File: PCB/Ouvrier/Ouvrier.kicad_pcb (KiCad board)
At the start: 2 copper layers, 52 x 54.5 mm, 17 parts, among them J1 Batterie, J2 VBAT Xiao, J3 DC 5V input, Q1 2N2222B, U1 XIAO-ESP32-S3-Plus-DIP, U2 BMP581, U3 UWB

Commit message: Ouvrier_V8
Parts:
- R3: value 330R -> 1k
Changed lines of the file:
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@@
 			)
 		)
-		(property "Value" "330R"
+		(property "Value" "1k"
 			(at 5.08 2.37 0)
 			(layer "F.Fab")

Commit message: gbr
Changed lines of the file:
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@@
 		(filling no)
 		(pcbplotparams
-			(layerselection 0x00000000_00000000_55555555_5755f5ff)
-			(plot_on_all_layers_selection 0x00000000_00000000_00000000_00000000)
+			(layerselection 0x00000000_00000000_55555555_57555555)
+			(plot_on_all_layers_selection 0x00000000_00000000_00000000_02000000)
 			(disableapertmacros no)
 			(usegerberextensions no)
@@
 			(outputformat 1)
 			(mirror no)
-			(drillshape 1)
+			(drillshape 0)
 			(scaleselection 1)
 			(outputdirectory "")
@@
 	(via
 		(at 141.5 90.5)
-		(size 1)
+		(size 1.1)
 		(drill 0.8)
 		(layers "F.Cu" "B.Cu")
@@
 	(via
 		(at 120.25 66.25)
-		(size 1)
+		(size 1.1)
 		(drill 0.8)
 		(layers "F.Cu" "B.Cu")

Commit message: Ouvrier_v9_changement_bmp
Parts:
- moved R3 26.9 mm to (122.9, 100.0)
- moved R1 25.2 mm to (96.0, 96.5), turned to 0 degrees
- moved LS2 17.2 mm to (115.0, 101.2)
- moved D2 8.94 mm to (133.0, 103.2), turned to -90 degrees
- moved U2 7.99 mm to (131.0, 93.0), turned to 180 degrees
- moved Q1 7.15 mm to (107.0, 102.8)
- moved D1 4.61 mm to (119.8, 86.4)
- moved C1 4.29 mm to (140.5, 96.0), turned to 90 degrees
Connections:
- U2 pad 2: Net-(U1-P1.13_D8_SCK) -> GNDREF
- U2 pad 3: GNDREF -> Net-(U1-P1.13_D8_SCK)
- U2 pad 5: Net-(U1-P1.14_D9_MISO) -> unconnected-(U2-INT-Pad5)
- U2 pad 7: unconnected-(U2-INT-Pad7) -> Net-(U1-P1.14_D9_MISO)
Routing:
- net Net-(D2-K): track 44.3 -> 3.28 mm
- net GNDREF: track 71.5 -> 38.3 mm, vias 1 -> 0
- net Net-(U1-P0.28_A2_D2): track 23.1 -> 47.7 mm
- net Net-(U1-P1.14_D9_MISO): track 45.6 -> 28.0 mm
- net +3V3: track 92.9 -> 105.5 mm
- net Net-(D1-A): track 15.0 -> 22.2 mm
- net Net-(U1-P0.29_A3_D3): track 27.1 -> 20.9 mm
- net Net-(U1-P0.04_A4_D4_SDA): track 42.9 -> 38.3 mm
- net Net-(Q1-B): track 8.28 -> 5.17 mm
- net Net-(U1-P1.13_D8_SCK): track 18.2 -> 19.7 mm
- net Net-(U1-P1.15_D10_MOSI): track 20.1 -> 18.8 mm
- net Net-(U1-P1.12_D7_RX): vias 1 -> 0

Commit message: Ouvrier_v10_PCB
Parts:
- removed C1: 100nF, Capacitor_SMD:C_0402_1005Metric_Pad0.74x0.62mm_HandSolder
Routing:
- net GNDREF: track 38.3 -> 35.2 mm
- net +3V3: track 105.5 -> 104.7 mm

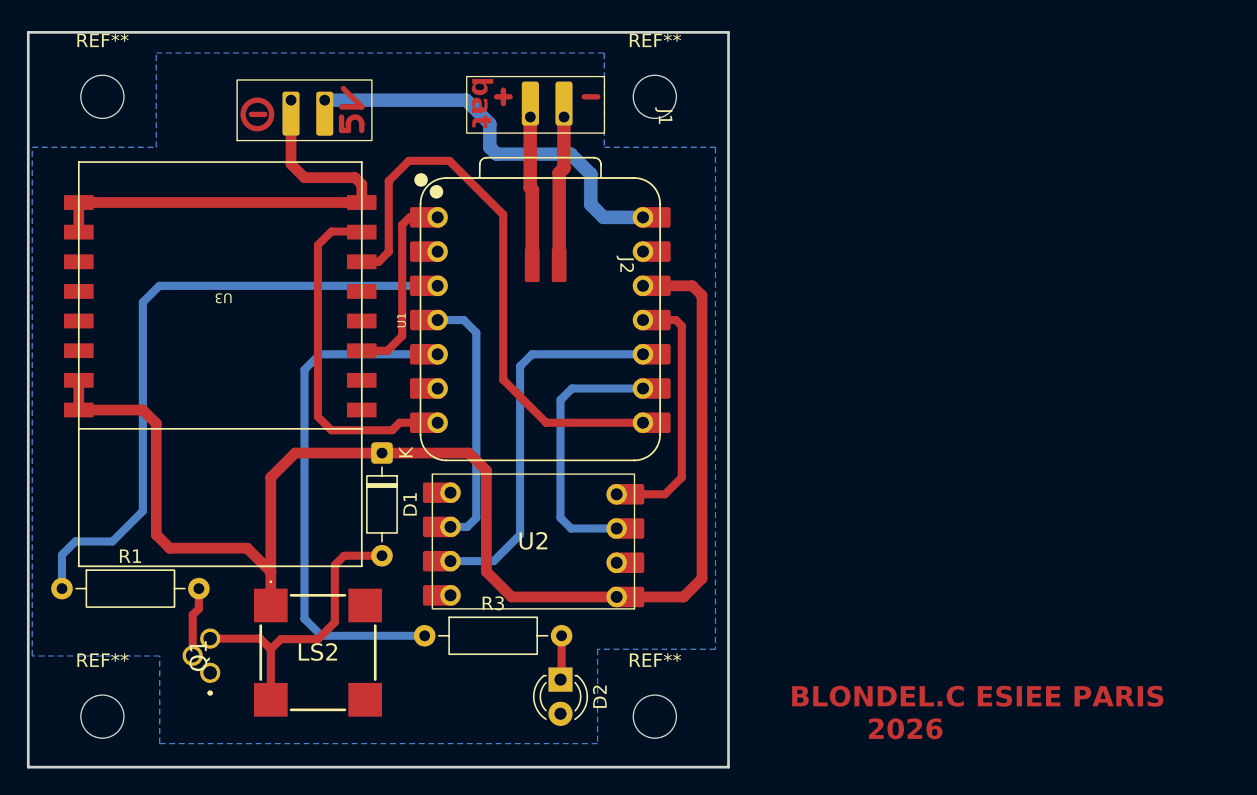
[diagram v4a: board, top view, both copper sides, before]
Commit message: MaJ KiCad Ouvrier
pin INT BMP et raccord batterie
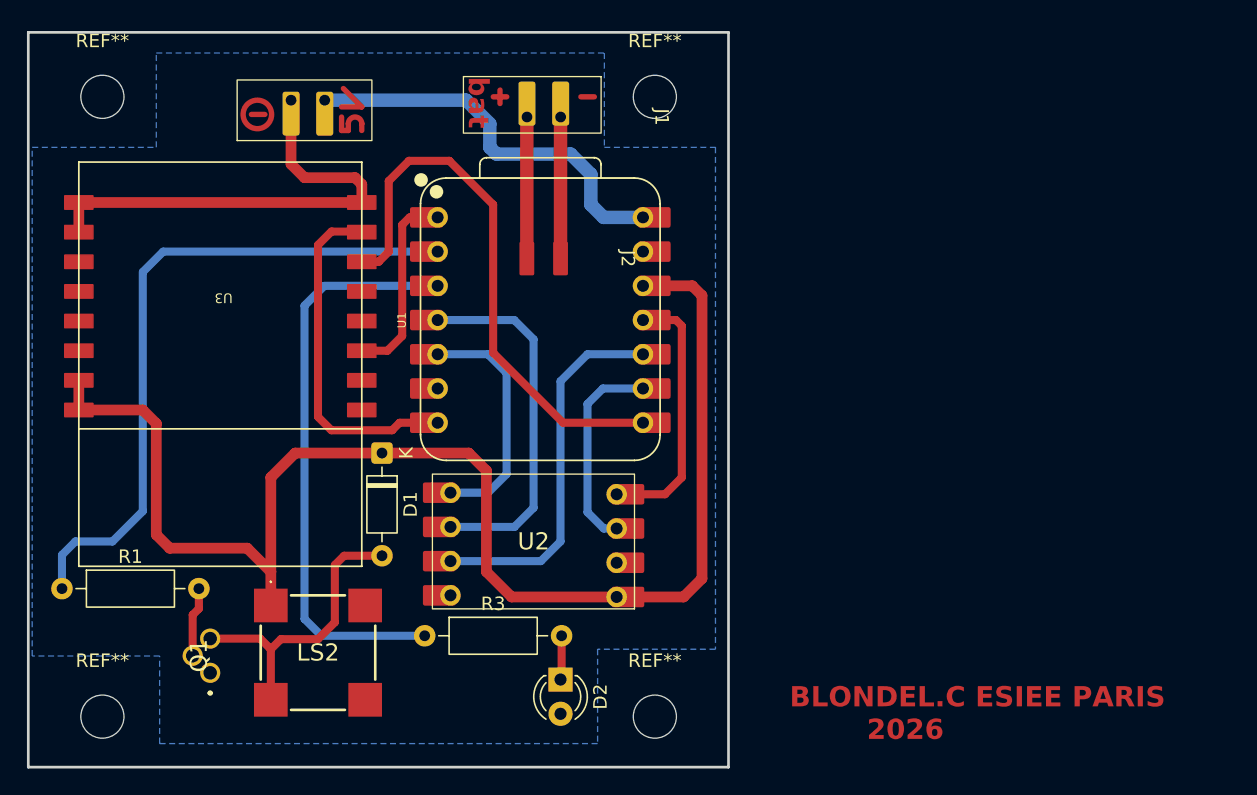
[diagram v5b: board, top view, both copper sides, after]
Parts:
- moved J2 0.51 mm to (137.5, 72.0)
- moved J1 0.25 mm to (140.0, 61.5)
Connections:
- R1 pad 1: Net-(U1-P0.28_A2_D2) -> Net-(U1-P0.03_A1_D1)
- R3 pad 1: Net-(U1-P0.04_A4_D4_SDA) -> Net-(U1-P0.28_A2_D2)
- U1 pad 2: unconnected-(U1-P0.03_A1_D1-Pad2) -> Net-(U1-P0.03_A1_D1)
- U2 pad 5: unconnected-(U2-INT-Pad5) -> Net-(U1-P0.04_A4_D4_SDA)
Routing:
- net Net-(U1-P0.03_A1_D1): track 0.00 -> 50.1 mm
- net Net-(U1-P0.04_A4_D4_SDA): track 38.3 -> 17.9 mm
- net Net-(U1-P0.29_A3_D3): track 20.9 -> 27.8 mm
- net Net-(U1-P0.28_A2_D2): track 47.7 -> 43.2 mm
- net Net-(U1-P1.13_D8_SCK): track 19.7 -> 15.3 mm
- net Net-(J1-Pin_2): track 11.3 -> 10.5 mm
- net Net-(U1-P1.12_D7_RX): track 42.3 -> 41.5 mm
- net Net-(J1-Pin_1): track 11.1 -> 10.5 mm
